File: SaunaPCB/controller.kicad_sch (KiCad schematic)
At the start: 5 parts, among them J3 KL2RM5.08, J4 KL2RM5.08, J5 KL2RM5.08, J6 KL2RM5.08, U4 ESP32-S3-DevKitC

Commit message: Working on schematic and PCB -AC/DC and DC/DC converters with correct symbol and footprint now - rough placement of the power parts
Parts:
- U4: footprint PCM_Espressif:ESP32-S3-DevKitC -> Espreessif ESP32:ESP32-S3-DevKitC
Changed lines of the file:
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@@
 			)
 		)
-		(property "Footprint" "PCM_Espressif:ESP32-S3-DevKitC"
+		(property "Footprint" "Espreessif ESP32:ESP32-S3-DevKitC"
 			(at 139.7 148.59 0)
 			(effects

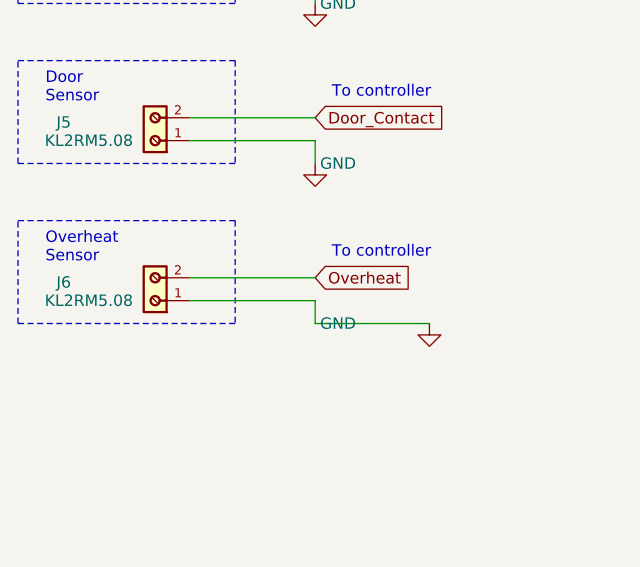
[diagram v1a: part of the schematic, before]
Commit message: Relay power supply changed
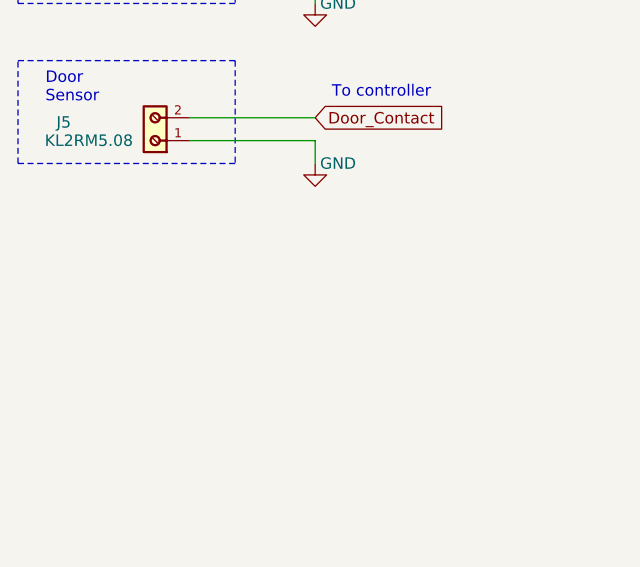
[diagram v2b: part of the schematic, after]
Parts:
- removed J6: KL2RM5.08, MyConnectors:Terminal_Block_2_RM5.08, symbol MyConnectors:Terminal_Block_2
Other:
- note removed: "Overheat Sensor"
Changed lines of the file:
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@@
-		)
-	)
-	(rectangle
-		(start 17.78 72.39)
-		(end 41.91 83.82)
-		(stroke
-			(width 0)
-			(type dash)
-		)
-		(fill
-			(type none)
 		)
 	)
@@
 		)
 	)
-	(text "Overheat\nSensor"
-		(exclude_from_sim no)
-		(at 20.828 75.438 0)
+	(text "To controller"
+		(exclude_from_sim no)
+		(at 58.166 22.606 0)
+		(effects
+			(font
+				(size 1.27 1.27)
+			)
+		)
+	)
+	(text "Door\nSensor"
+		(exclude_from_sim no)
+		(at 20.828 57.658 0)
 		(effects
 			(font
@@
 	(text "To controller"
 		(exclude_from_sim no)
-		(at 58.166 22.606 0)
-		(effects
-			(font
-				(size 1.27 1.27)
-			)
-		)
-	)
-	(text "Door\nSensor"
-		(exclude_from_sim no)
-		(at 20.828 57.658 0)
-		(effects
-			(font
-				(size 1.27 1.27)
-			)
-			(justify left)
+		(at 58.166 58.166 0)
+		(effects
+			(font
+				(size 1.27 1.27)
+			)
 		)
 	)
 	(text "To controller"
 		(exclude_from_sim no)
-		(at 58.166 58.166 0)
-		(effects
-			(font
-				(size 1.27 1.27)
-			)
-		)
-	)
-	(text "To controller"
-		(exclude_from_sim no)
-		(at 58.166 75.946 0)
-		(effects
-			(font
-				(size 1.27 1.27)
-			)
-		)
-	)
-	(text "To controller"
-		(exclude_from_sim no)
 		(at 58.166 40.386 0)
 		(effects
@@
 	(wire
 		(pts
-			(xy 50.8 83.82) (xy 63.5 83.82)
-		)
-		(stroke
-			(width 0)
-			(type default)
-		)
-	)
-	(wire
-		(pts
-			(xy 36.83 78.74) (xy 50.8 78.74)
-		)
-		(stroke
-			(width 0)
-			(type default)
-		)
-	)
-	(wire
-		(pts
 			(xy 139.7 137.16) (xy 139.7 139.7)
 		)
@@
 	(wire
 		(pts
-			(xy 50.8 81.28) (xy 50.8 83.82)
-		)
-		(stroke
-			(width 0)
-			(type default)
-		)
-	)
-	(wire
-		(pts
 			(xy 36.83 27.94) (xy 50.8 27.94)
 		)
@@
 		(pts
 			(xy 36.83 63.5) (xy 50.8 63.5)
-		)
-		(stroke
-			(width 0)
-			(type default)
-		)
-	)
-	(wire
-		(pts
-			(xy 36.83 81.28) (xy 50.8 81.28)
 		)
 		(stroke
@@
 		)
 	)
-	(global_label "Overheat"
-		(shape input)
-		(at 50.8 78.74 0)
-		(fields_autoplaced yes)
-		(effects
-			(font
-				(size 1.27 1.27)
-			)
-			(justify left)
-		)
-		(property "Intersheetrefs" "${INTERSHEET_REFS}"
-			(at 66.364 78.74 0)
-			(effects
-				(font
-					(size 1.27 1.27)
-				)
-				(justify left)
-				(hide yes)
-			)
-		)
-	)
 	(global_label "Door_Contact"
 		(shape input)
@@
 				(justify left)
 				(hide yes)
-			)
-		)
-	)
-	(symbol
-		(lib_id "power:GND")
-		(at 63.5 83.82 0)
-		(unit 1)
-		(exclude_from_sim no)
-		(in_bom yes)
-		(on_board yes)
-		(dnp no)
-		(property "Reference" "#PWR016"
-			(at 63.5 90.17 0)
-			(effects
-				(font
-					(size 1.27 1.27)
-				)
-				(hide yes)
-			)
-		)
-		(property "Value" "GND"
-			(at 53.34 83.82 0)
-			(effects
-				(font
-					(size 1.27 1.27)
-				)
-			)
-		)
-		(property "Footprint" ""
-			(at 63.5 83.82 0)
-			(effects
-				(font
-					(size 1.27 1.27)
-				)
-				(hide yes)
-			)
-		)
-		(property "Datasheet" ""
-			(at 63.5 83.82 0)
-			(effects
-				(font
-					(size 1.27 1.27)
-				)
-				(hide yes)
-			)
-		)
-		(property "Description" "Power symbol creates a global label with name \"GND\" , ground"
-			(at 63.5 83.82 0)
-			(effects
-				(font
-					(size 1.27 1.27)
-				)
-				(hide yes)
-			)
-		)
-		(pin "1"
-		)
-		(instances
-			(project "SaunaPCB"
-				(path "/e6d8484d-2bb5-441d-9b2b-e37a9f2fa458/8da01db6-a1a1-4b01-9382-9f6e5fdc0347"
-					(reference "#PWR016")
-					(unit 1)
-				)
 			)
 		)
@@
 					(unit 1)
 				)
-			)
-		)
-	)
-	(symbol
-		(lib_id "MyConnectors:Terminal_Block_2")
-		(at 36.83 81.28 90)
-		(unit 1)
-		(exclude_from_sim no)
-		(in_bom yes)
-		(on_board yes)
-		(dnp no)
-		(property "Reference" "J6"
-			(at 22.86 79.248 90)
-			(effects
-				(font
-					(size 1.27 1.27)
-				)
-			)
-		)
-		(property "Value" "KL2RM5.08"
-			(at 25.654 81.28 90)
-			(effects
-				(font
-					(size 1.27 1.27)
-				)
-			)
-		)
-		(property "Footprint" "MyConnectors:Terminal_Block_2_RM5.08"
-			(at 36.83 81.28 0)
-			(effects
-				(font
-					(size 1.27 1.27)
-				)
-				(hide yes)
-			)
-		)
-		(property "Datasheet" ""
-			(at 36.83 81.28 0)
-			(effects
-				(font
-					(size 1.27 1.27)
-				)
-				(hide yes)
-			)
-		)
-		(property "Description" "2 pol screw terminal"
-			(at 36.83 81.28 0)
-			(effects
-				(font
-					(size 1.27 1.27)
-				)
-				(hide yes)
-			)
-		)
-		(pin "2"
-		)
-		(pin "1"
-		)
-		(instances
-			(project "SaunaPCB"
-				(path "/e6d8484d-2bb5-441d-9b2b-e37a9f2fa458/8da01db6-a1a1-4b01-9382-9f6e5fdc0347"
-					(reference "J6")
-					(unit 1)
-				)

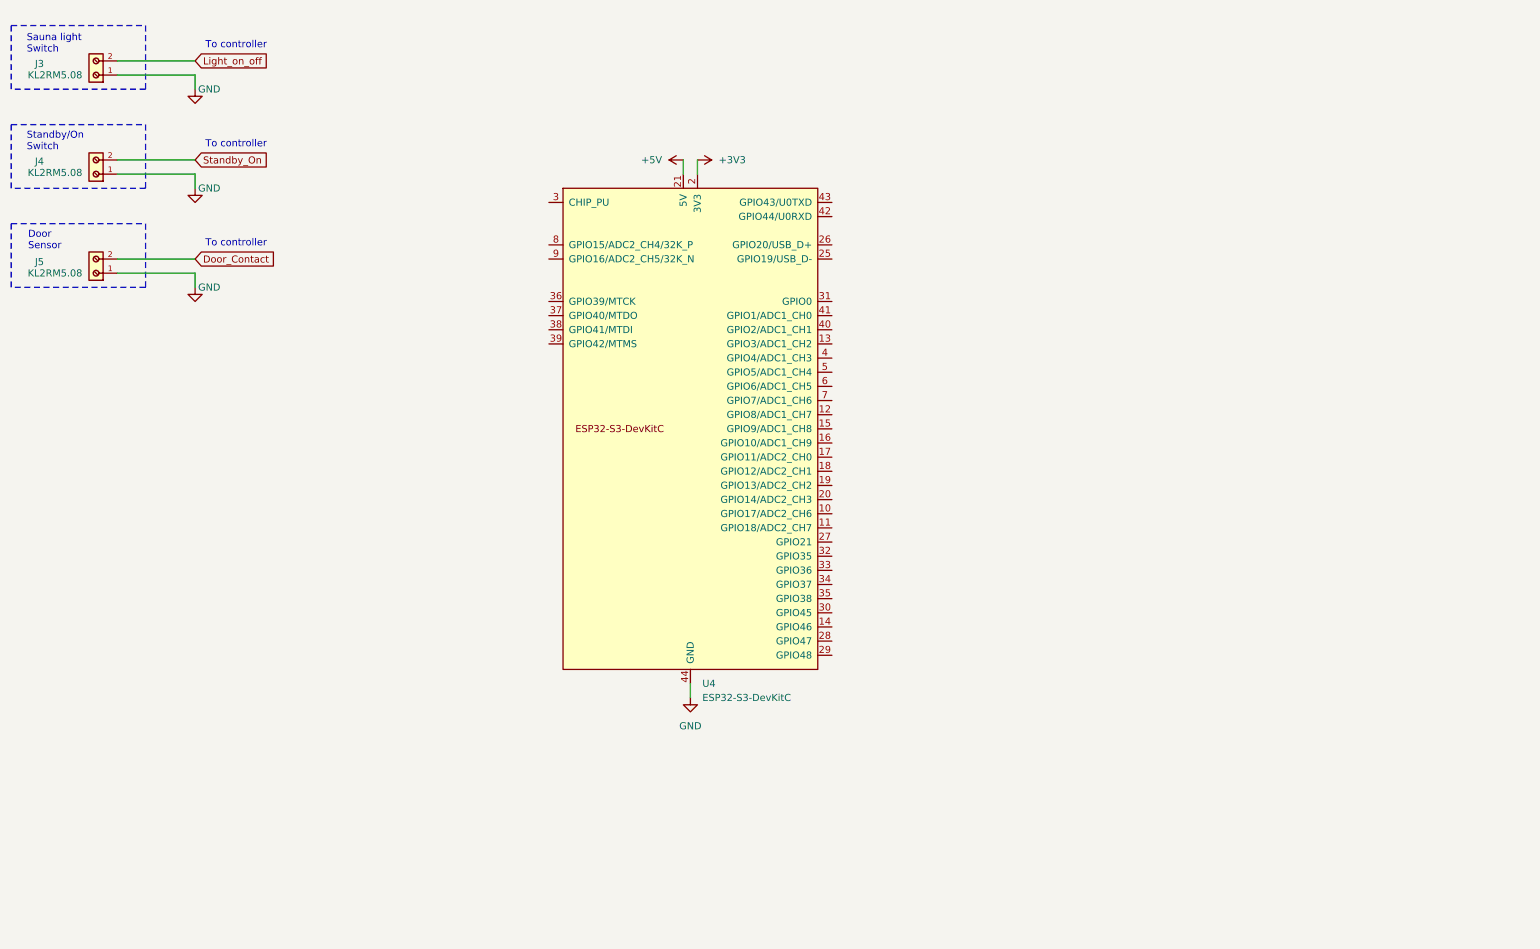
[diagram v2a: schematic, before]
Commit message: Working on schematic: - Own ESP32 Devkit V4 device used. - ESP32 connections added (all signals from page on connected)
- Next steps: Connection to LCD, Relay driver, Encoder Interface and standby LED
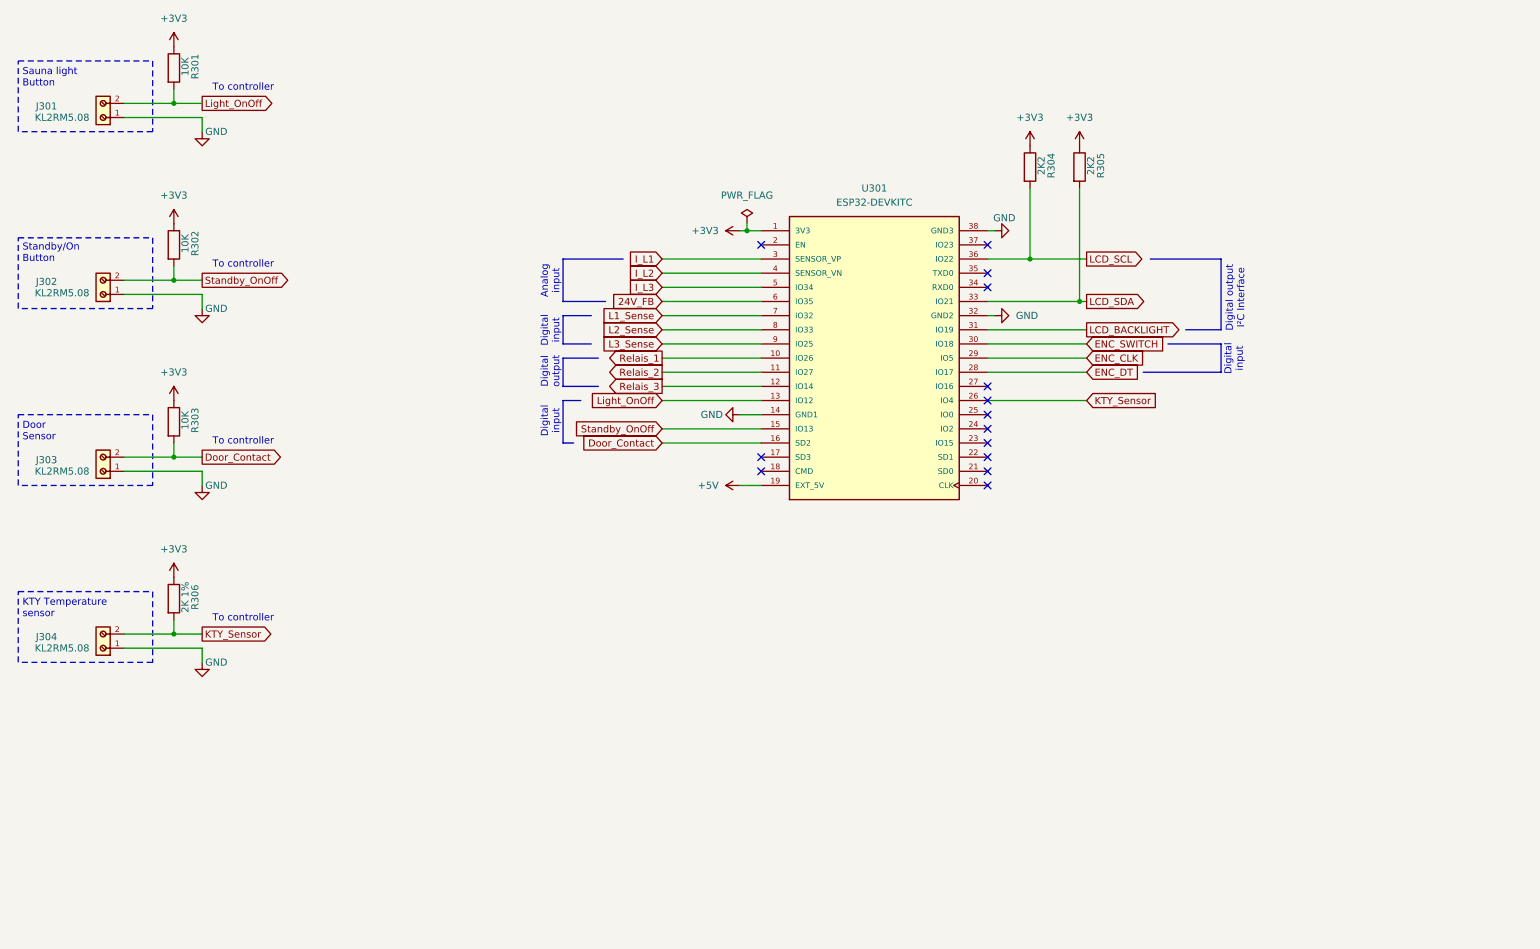
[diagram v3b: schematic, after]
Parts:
- removed U4: ESP32-S3-DevKitC, Espreessif ESP32:ESP32-S3-DevKitC, symbol Espressif ESP32:ESP32-S3-DevKitC
- added J304: KL2RM5.08, MyConnectors:Terminal_Block_2_RM5.08, symbol MyConnectors:Terminal_Block_2
- added R301, R302, R303: 10K, Resistor_SMD:R_1206_3216Metric, symbol Device:R
- added R304, R305: 2K2, Resistor_SMD:R_1206_3216Metric, symbol Device:R
- added R306: 2K 1%, Resistor_SMD:R_1206_3216Metric, symbol Device:R
- added U301: ESP32-DEVKITC, MyESP32:ESP32_DevKit_V4, symbol MyESP32:ESP32-DEVKITC
- renumbered J3 to J301, J4 to J302, J5 to J303
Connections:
- net +3V3: now also R301.1, R302.1, R303.1, R304.1, R305.1, R306.1, U301.1 (3V3)
- net +5V: now also U301.19 (EXT_5V)
- net Door_Contact: now also R303.2, U301.16 (SD2)
- net GND: now also J304.1, U301.14 (GND1), U301.32 (GND2), U301.38 (GND3)
- net Light_on_off renamed Light_OnOff
- net Light_OnOff: now also R301.2, U301.13 (IO12)
- net Standby_On renamed Standby_OnOff
- net Standby_OnOff: now also R302.2, U301.15 (IO13)
- new net 24V_FB: U301.6 (IO35)
- new net ENC_CLK: U301.29 (IO5)
- new net ENC_DT: U301.28 (IO17)
- new net ENC_SWITCH: U301.30 (IO18)
- new net I_L1: U301.3 (SENSOR_VP)
- new net I_L2: U301.4 (SENSOR_VN)
- new net I_L3: U301.5 (IO34)
- new net KTY_Sensor: J304.2, R306.2, U301.26 (IO4)
- new net L1_Sense: U301.7 (IO32)
- new net L2_Sense: U301.8 (IO33)
- new net L3_Sense: U301.9 (IO25)
- new net LCD_BACKLIGHT: U301.31 (IO19)
- new net LCD_SCL: R304.2, U301.36 (IO22)
- new net LCD_SDA: R305.2, U301.33 (IO21)
- new net Relais_1: U301.10 (IO26)
- new net Relais_2: U301.11 (IO27)
- new net Relais_3: U301.12 (IO14)
- no-connect marks 0 -> 14
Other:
- note added: "Analog input"
- note added: "Digital input"
- note added: "Digital output"
- note added: "Digital output I²C Interface"
- note added: "KTY Temperature sensor"
- note added: "Sauna light Button"
- note added: "Standby/On Button"
- note removed: "Sauna light Switch"
- note removed: "Standby/On Switch"
- moved on the sheet: J301, J302, J303

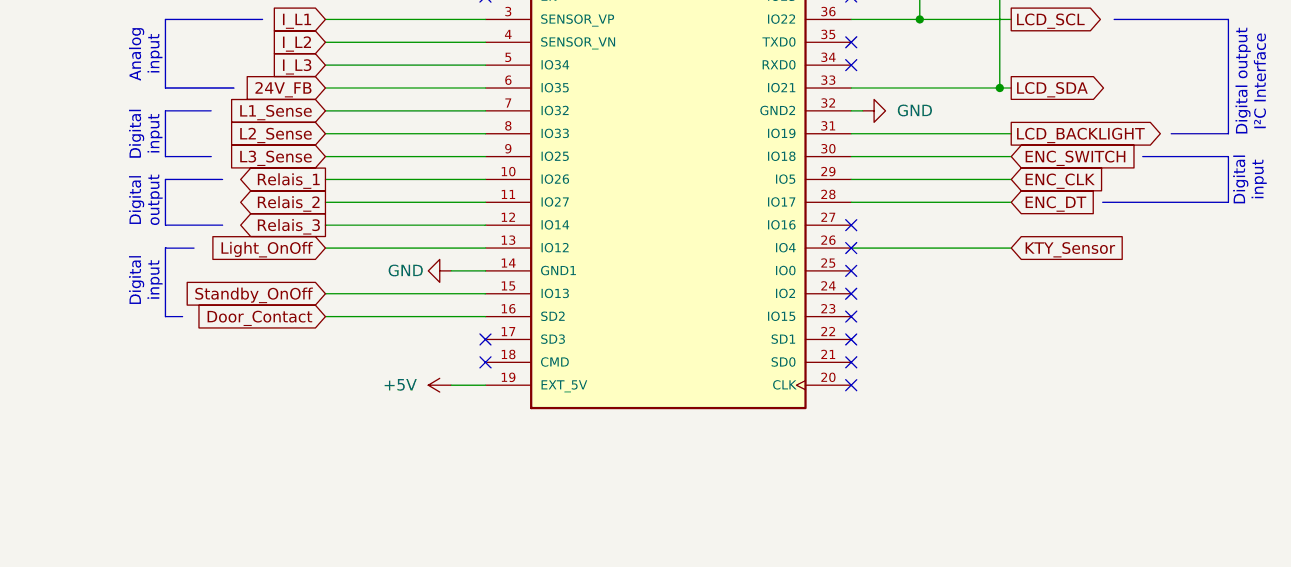
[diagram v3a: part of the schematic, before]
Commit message: Minor changes on port usage
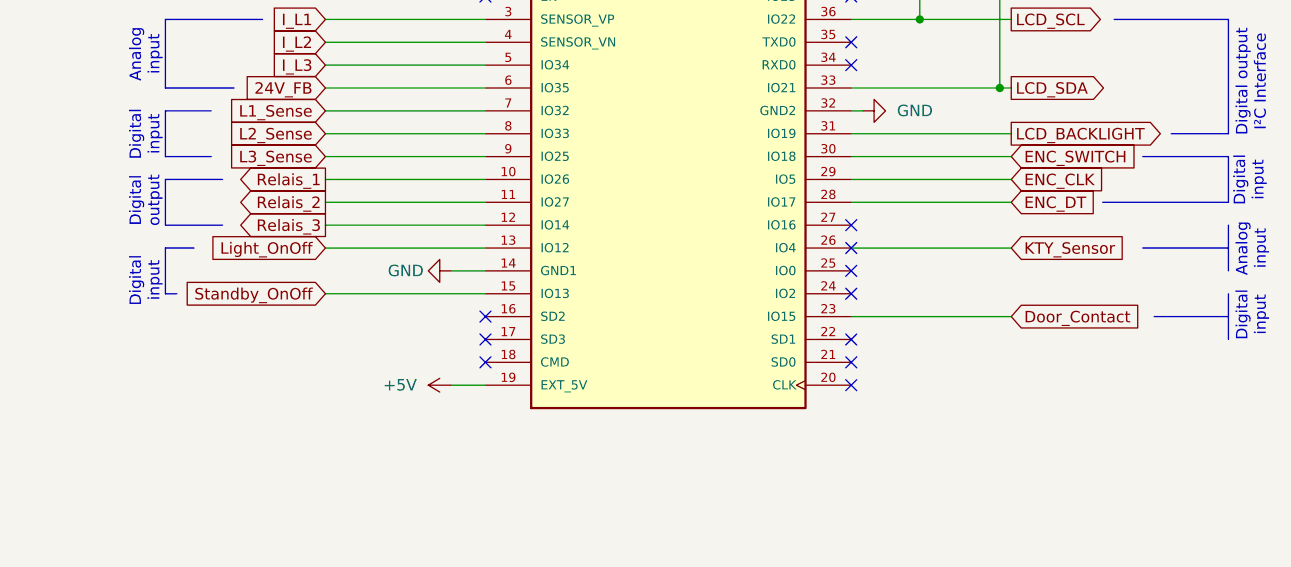
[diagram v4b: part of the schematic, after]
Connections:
- net Door_Contact: now also U301.23 (IO15); no longer U301.16 (SD2)
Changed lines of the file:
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@@
+		)
+	)
+	(text "Analog\ninput"
+		(exclude_from_sim no)
+		(at 237.49 86.614 90)
+		(effects
+			(font
+				(size 1.27 1.27)
+			)
 		)
 	)
@@
 		(exclude_from_sim no)
 		(at 59.436 30.226 0)
+		(effects
+			(font
+				(size 1.27 1.27)
+			)
+		)
+	)
+	(text "Digital\ninput"
+		(exclude_from_sim no)
+		(at 237.49 93.98 90)
 		(effects
 			(font
@@
 	)
 	(no_connect
-		(at 193.04 93.98)
-	)
-	(no_connect
 		(at 193.04 99.06)
 	)
@@
 	)
 	(no_connect
+		(at 152.4 93.98)
+	)
+	(no_connect
 		(at 152.4 58.42)
 	)
@@
 	(polyline
 		(pts
-			(xy 116.84 86.36) (xy 116.84 93.98)
+			(xy 116.84 86.36) (xy 116.84 91.44)
 		)
 		(stroke
@@
 		)
 	)
+	(polyline
+		(pts
+			(xy 225.425 86.36) (xy 234.95 86.36)
+		)
+		(stroke
+			(width 0)
+			(type default)
+		)
+	)
 	(wire
 		(pts
@@
 	(polyline
 		(pts
-			(xy 116.84 93.98) (xy 118.745 93.98)
+			(xy 116.84 91.44) (xy 118.11 91.44)
 		)
 		(stroke
@@
 	(wire
 		(pts
-			(xy 134.62 93.98) (xy 152.4 93.98)
-		)
-		(stroke
-			(width 0)
-			(type default)
-		)
-	)
-	(wire
-		(pts
 			(xy 193.04 60.96) (xy 200.66 60.96)
 		)
@@
 		)
 	)
+	(polyline
+		(pts
+			(xy 226.695 93.98) (xy 234.95 93.98)
+		)
+		(stroke
+			(width 0)
+			(type default)
+		)
+	)
 	(wire
 		(pts
@@
 		)
 	)
+	(polyline
+		(pts
+			(xy 234.95 91.44) (xy 234.95 96.52)
+		)
+		(stroke
+			(width 0)
+			(type default)
+		)
+	)
 	(wire
 		(pts
@@
 	(wire
 		(pts
+			(xy 193.04 93.98) (xy 210.82 93.98)
+		)
+		(stroke
+			(width 0)
+			(type default)
+		)
+	)
+	(wire
+		(pts
 			(xy 46.99 62.23) (xy 46.99 64.77)
 		)
@@
 		(pts
 			(xy 134.62 60.96) (xy 152.4 60.96)
+		)
+		(stroke
+			(width 0)
+			(type default)
+		)
+	)
+	(polyline
+		(pts
+			(xy 234.95 83.82) (xy 234.95 88.9)
 		)
 		(stroke
@@
 	(global_label "Door_Contact"
 		(shape input)
-		(at 134.62 93.98 180)
-		(fields_autoplaced yes)
-		(effects
-			(font
-				(size 1.27 1.27)
-			)
-			(justify right)
-		)
-		(property "Intersheetrefs" "${INTERSHEET_REFS}"
-			(at 119.056 93.98 0)
-			(effects
-				(font
-					(size 1.27 1.27)
-				)
-				(justify right)
-				(hide yes)
-			)
+		(at 210.82 93.98 0)
+		(fields_autoplaced yes)
+		(effects
+			(font
+				(size 1.27 1.27)
+			)
+			(justify left)
+		)
+		(property "Intersheetrefs" "${INTERSHEET_REFS}"
+			(at 226.384 93.98 0)
+			(effects
+				(font
+					(size 1.27 1.27)
+				)
+				(justify left)
+				(hide yes)
+			)
